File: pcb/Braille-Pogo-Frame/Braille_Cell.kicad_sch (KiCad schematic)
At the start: 9 parts, among them J4 Conn_01x06, M4 Stepper_Motor_bipolar, U4 DRV8847SPWR

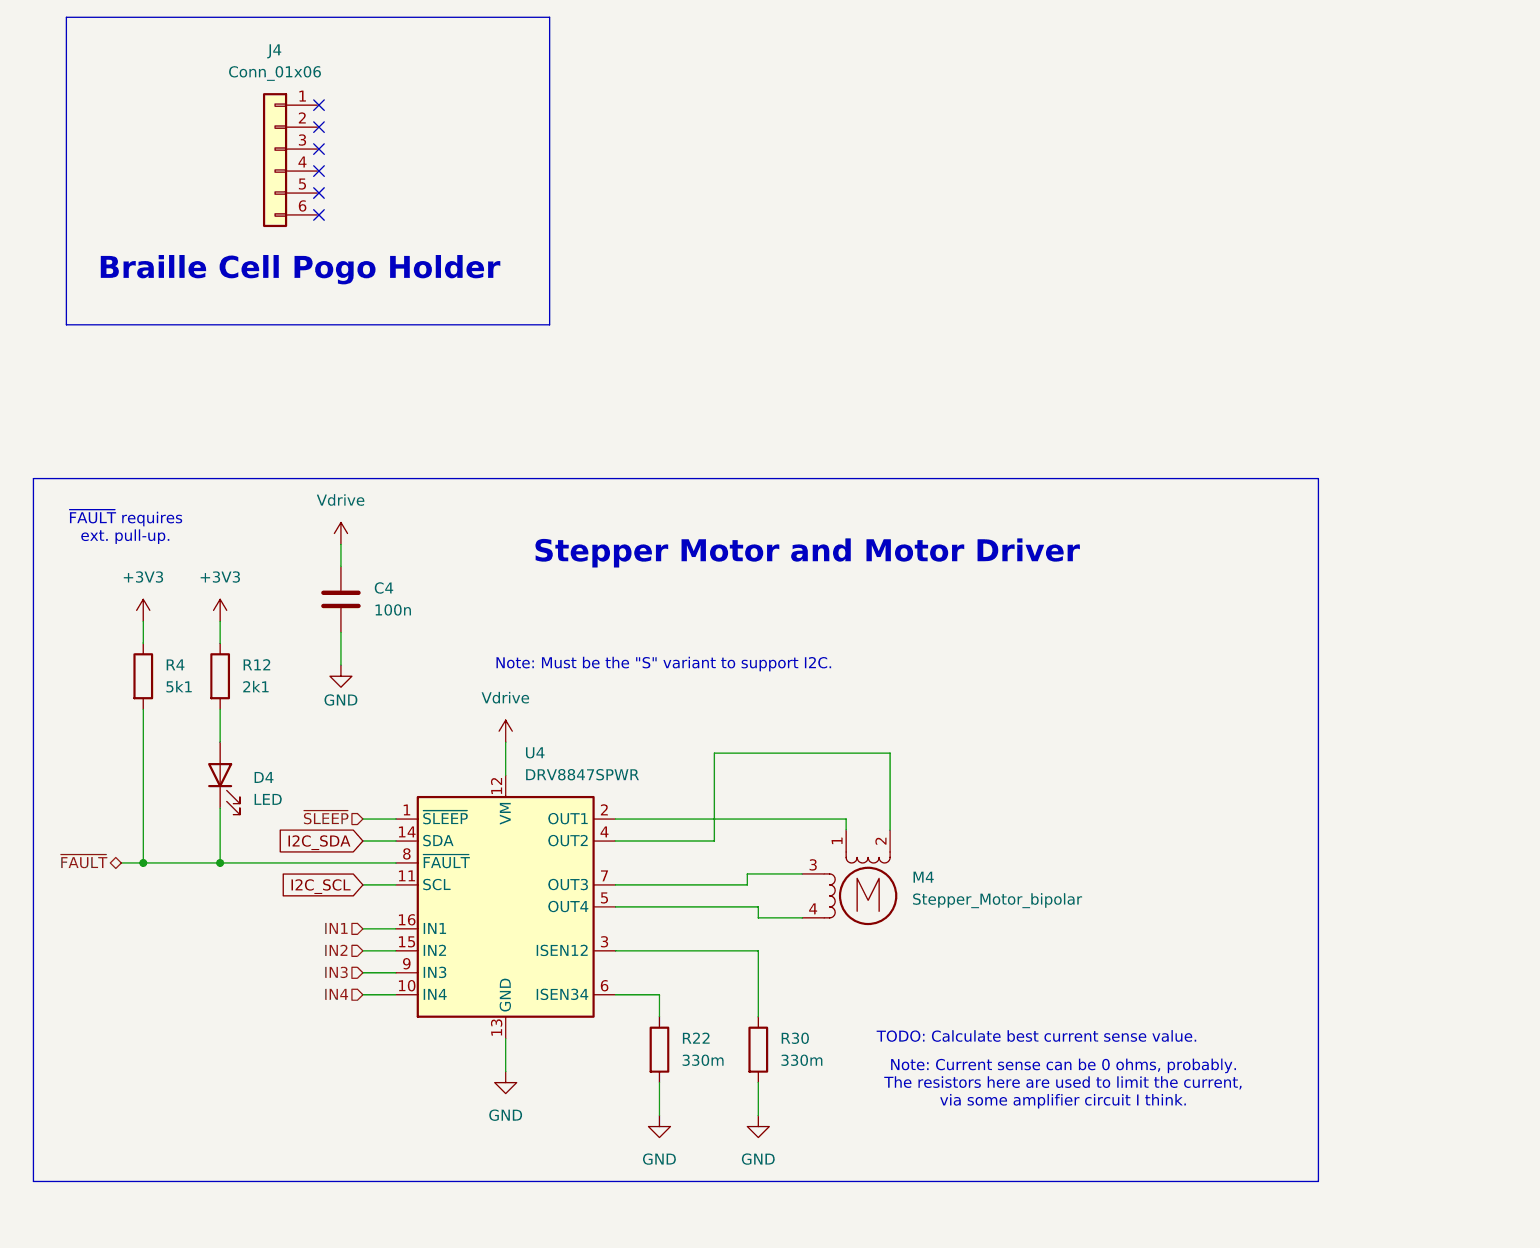
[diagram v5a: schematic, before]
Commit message: Add current sense comments to schematic
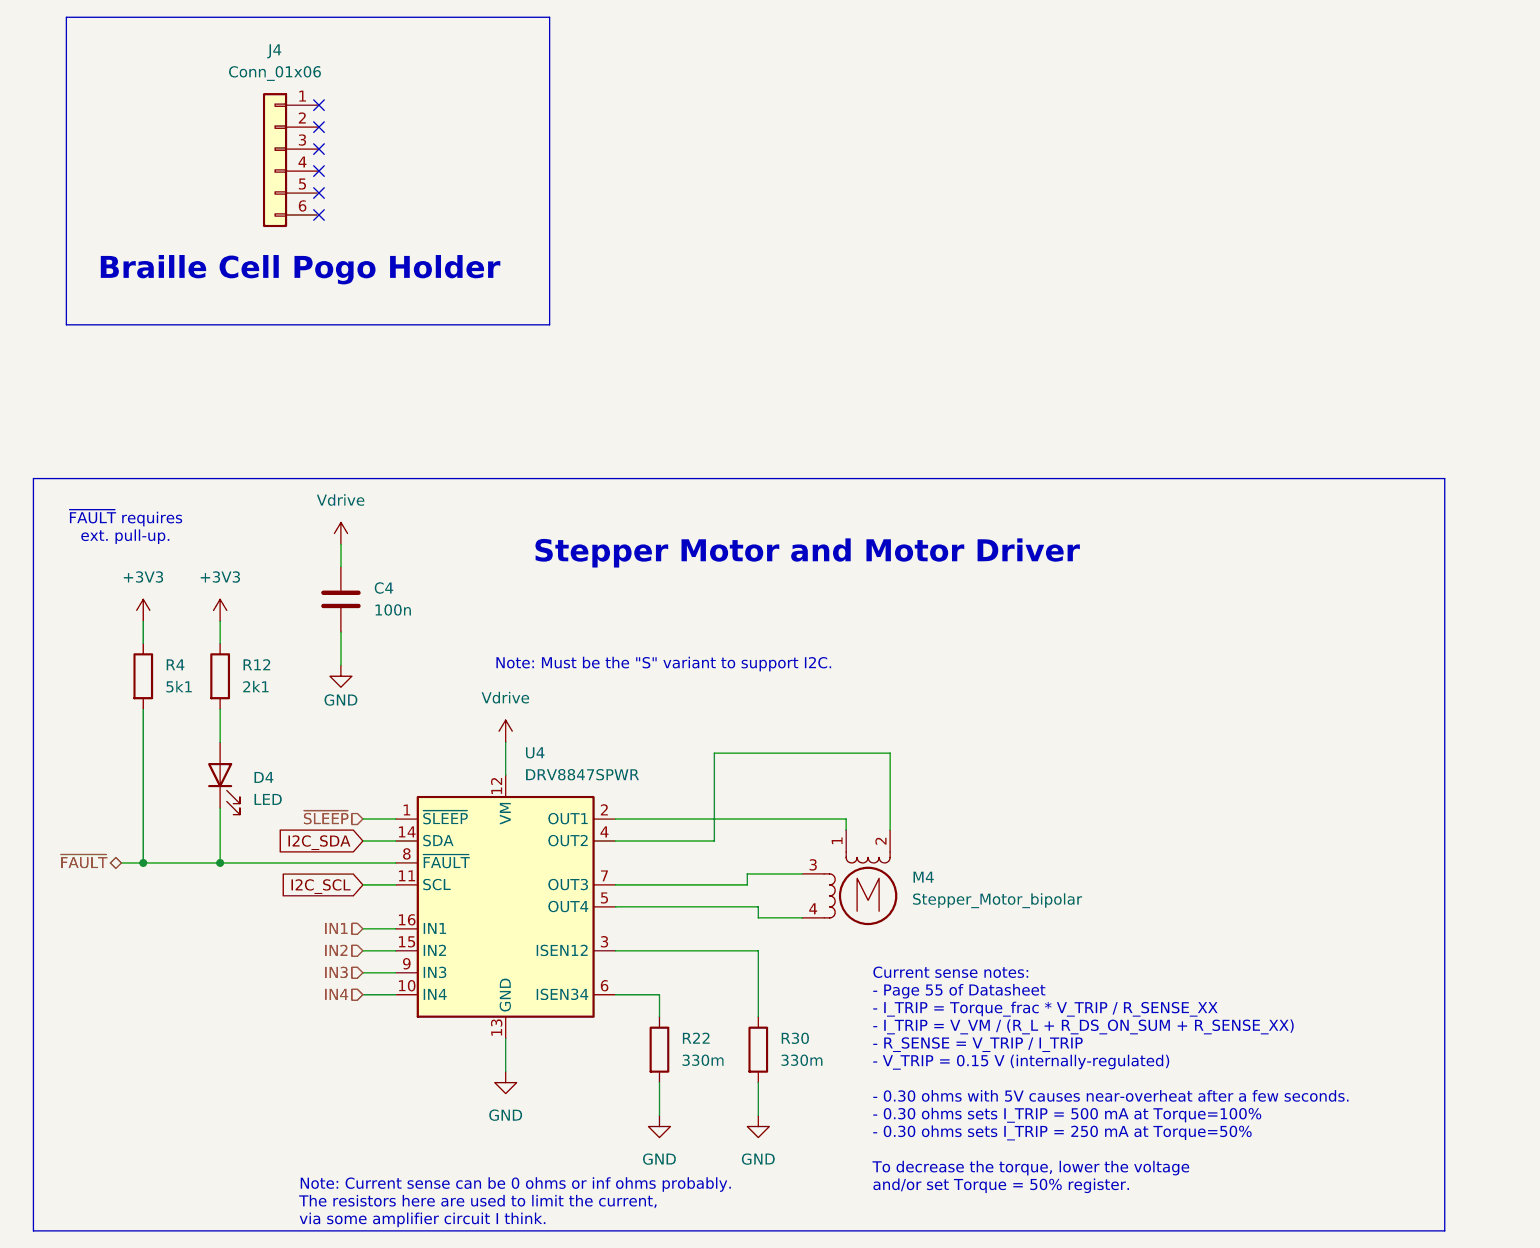
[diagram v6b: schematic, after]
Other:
- note added: "Current sense notes: - Page 55 of Datasheet - I_TRIP = Torque_frac * V_TRIP / R_SENSE_XX - I_TRIP = V_VM / (R_L + R_DS_ON_SUM + R_SENSE_XX) - R_SENSE = V_TRIP / I_TRIP - V_TRIP = 0.15 V (internally-regulated) - 0.30 ohms with 5V causes near-overheat after a few seconds. - 0.30 ohms sets I_TRIP = 500 mA at Torque=100% - 0.30 ohms sets I_TRIP = 250 mA at Torque=50% To decrease the torque, lower the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"
- note added: "Note: Current sense can be 0 ohms or inf ohms probably. The resistors here are used to limit the current, via some amplifier circuit I think."
- note removed: "Note: Current sense can be 0 ohms, probably. The resistors here are used to limit the current, via some amplifier circuit I think."
- note removed: "TODO: Calculate best current sense value."
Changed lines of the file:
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@@
 	(rectangle
 		(start 30.48 78.74)
-		(end 179.07 160.02)
+		(end 193.675 165.735)
 		(stroke
 			(width 0)
@@
 		)
 	)
-	(text "Note: Current sense can be 0 ohms, probably.\nThe resistors here are used to limit the current,\nvia some amplifier circuit I think."
+	(text "Note: Current sense can be 0 ohms or inf ohms probably.\nThe resistors here are used to limit the current,\nvia some amplifier circuit I think."
 		(exclude_from_sim no)
-		(at 149.606 148.844 0)
+		(at 61.214 162.56 0)
 		(effects
 			(font
@@
 				(thickness 0.1588)
 			)
+			(justify left)
 		)
 	)
-	(text "TODO: Calculate best current sense value."
+	(text "Current sense notes:\n- Page 55 of Datasheet\n- I_TRIP = Torque_frac * V_TRIP / R_SENSE_XX\n- I_TRIP = V_VM / (R_L + R_DS_ON_SUM + R_SENSE_XX)\n- R_SENSE = V_TRIP / I_TRIP\n- V_TRIP = 0.15 V (internally-regulated)\n\n- 0.30 ohms with 5V causes near-overheat after a few seconds.\n- 0.30 ohms sets I_TRIP = 500 mA at Torque=100%\n- 0.30 ohms sets I_TRIP = 250 mA at Torque=50%\n\nTo decrease the torque, lower the voltage\nand/or set Torque = 50% register."
 		(exclude_from_sim no)
-		(at 146.558 143.51 0)
+		(at 127.508 135.382 0)
 		(effects
 			(font
@@
 				(thickness 0.1588)
 			)
+			(justify left top)
 		)
 	)
